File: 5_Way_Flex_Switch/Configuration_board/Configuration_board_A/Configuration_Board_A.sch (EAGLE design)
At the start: 1 part

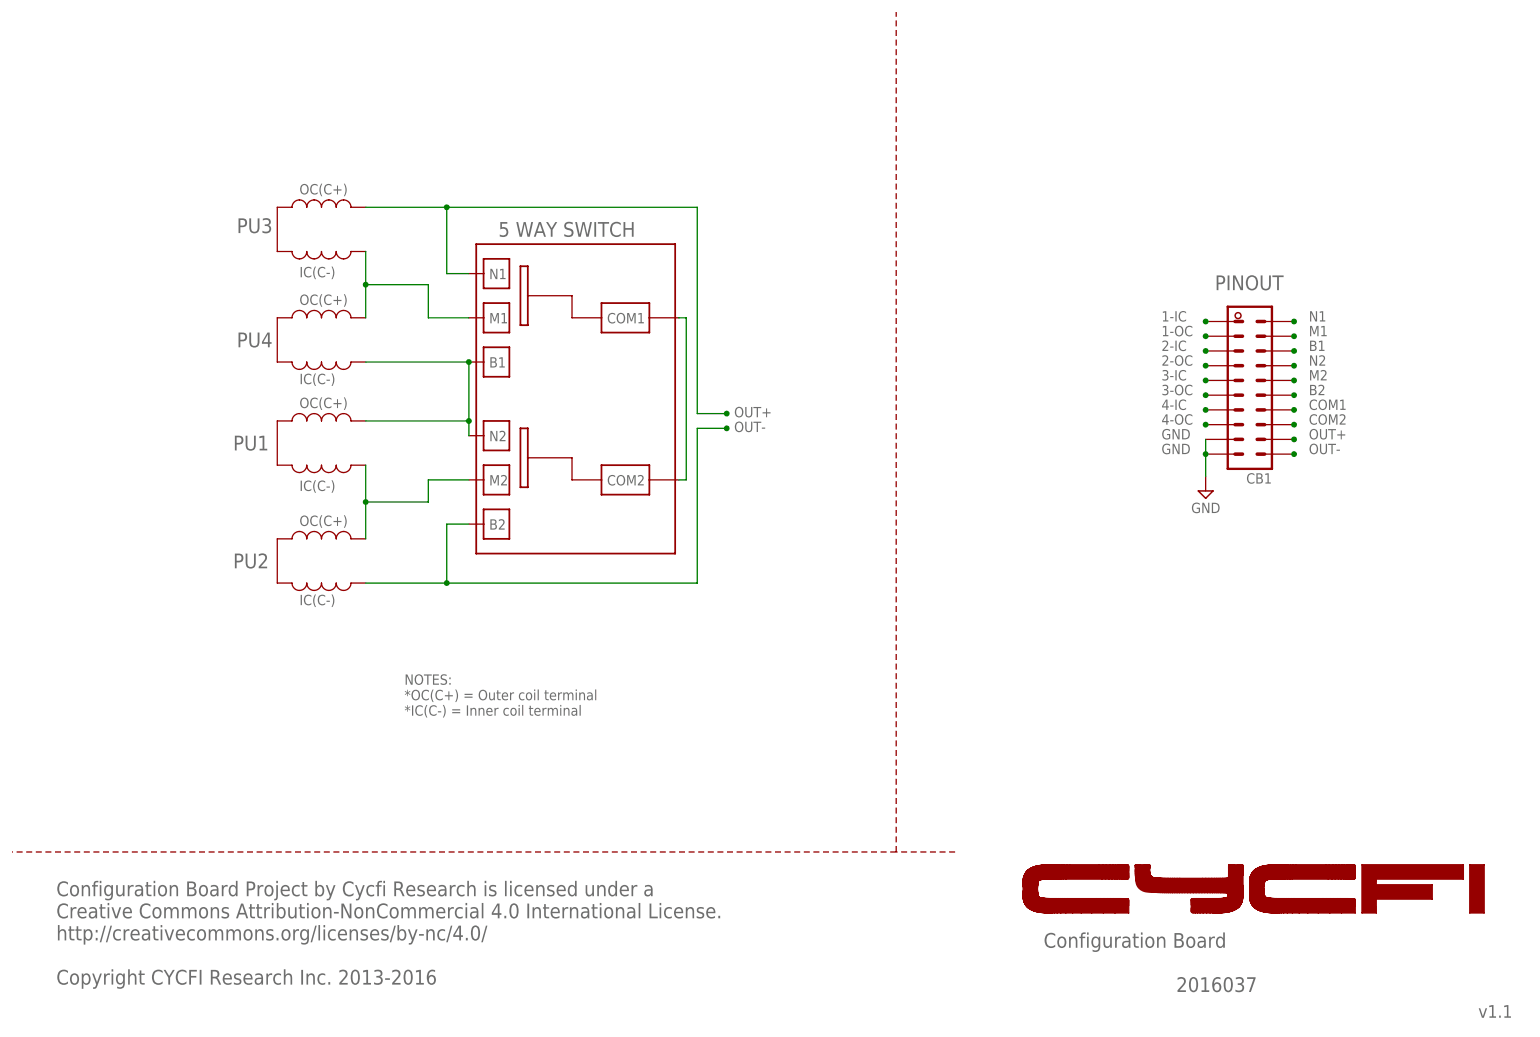
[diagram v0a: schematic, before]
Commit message: *organize 5-waay switch and its configuration board(a and b) *update license date *remove red frame schem pdf files, change with black frame *update document number
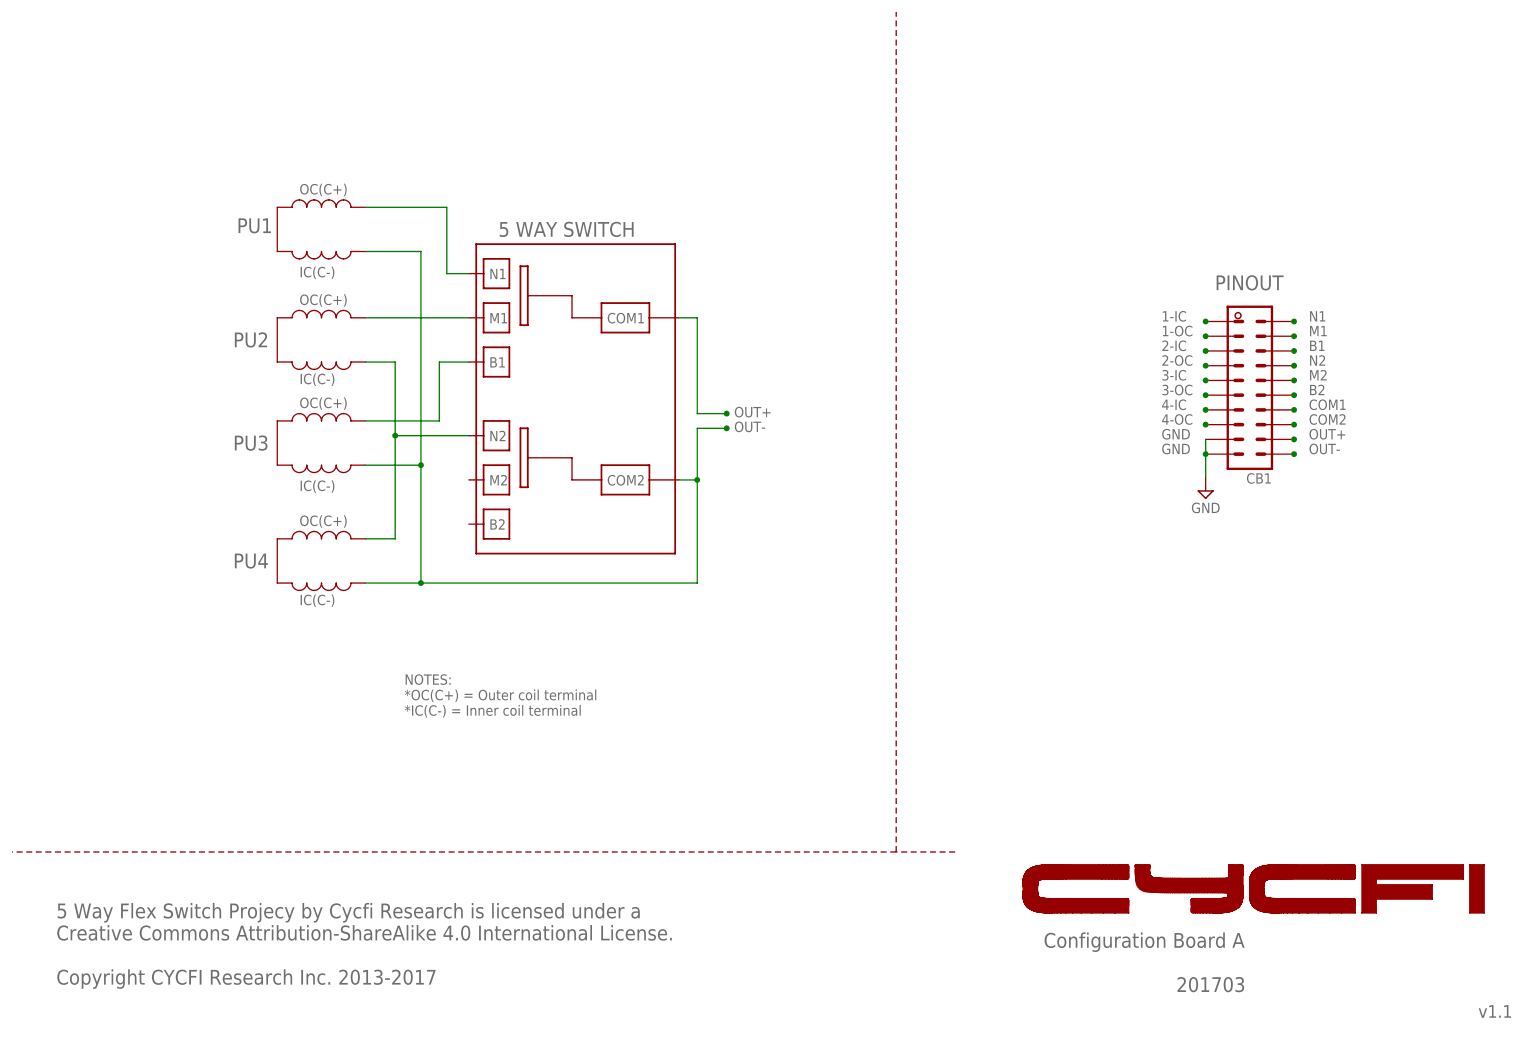
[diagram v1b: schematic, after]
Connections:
- removed net 1: CB1.3-OC, CB1.N1, CB1.OUT+
- removed net 2: CB1.3-IC, CB1.4-OC, CB1.M1
- removed net 3: CB1.1-OC, CB1.4-IC, CB1.B1, CB1.N2
- removed net 4: CB1.COM1, CB1.COM2
- removed net 5: CB1.1-IC, CB1.2-OC, CB1.M2
- removed net GND: CB1.GND, CB1.GND1
- new net B1: CB1.3-OC, CB1.B1
- new net B2: CB1.B2
- new net M1: CB1.2-OC, CB1.M1
- new net M2: CB1.M2
- new net N1: CB1.1-OC, CB1.N1
- new net N2: CB1.2-IC, CB1.4-OC, CB1.N2
- new net O+: CB1.COM1, CB1.OUT+
- new net O-: CB1.1-IC, CB1.3-IC, CB1.4-IC, CB1.COM2, CB1.OUT-
- net 6: now also CB1.GND, CB1.GND1; no longer CB1.2-IC, CB1.B2, CB1.OUT-
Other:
- note added: "201703"
- note added: "5 Way Flex Switch Projecy by Cycfi Research is licensed under a Creative Commons Attribution-ShareAlike 4.0 International License. Copyright CYCFI Research Inc. 2013-2017"
- note added: "Configuration Board A"
- note removed: "2016037"
- note removed: "Configuration Board"
- note removed: "Configuration Board Project by Cycfi Research is licensed under a Creative Commons Attribution-NonCommercial 4.0 International License. http://creativecommons.org/licenses/by-nc/4.0/ Copyright CYCFI Research Inc. 2013-2016"

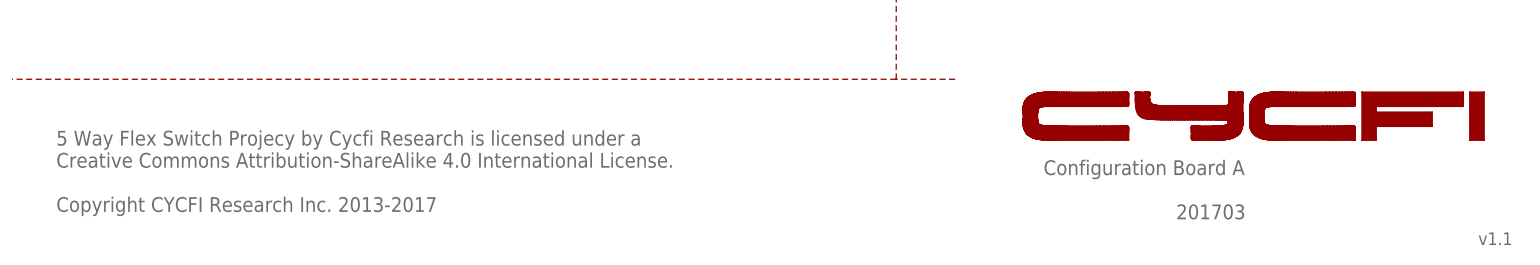
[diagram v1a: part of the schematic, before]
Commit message: Updated broken .sch files
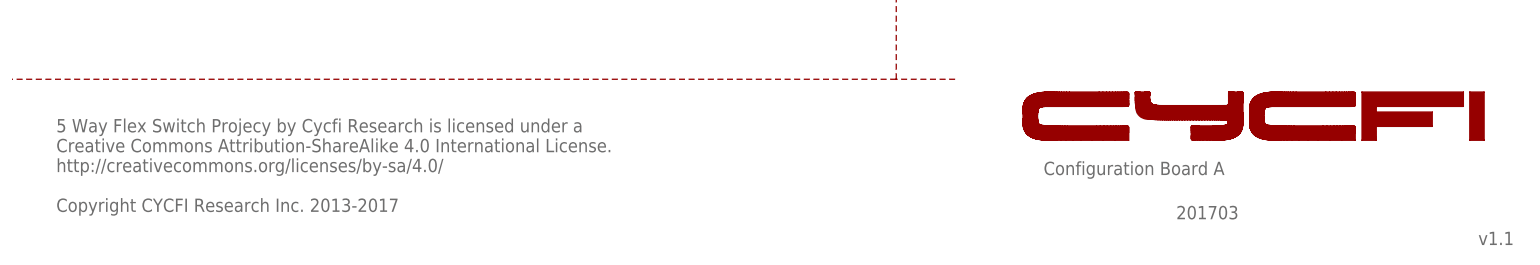
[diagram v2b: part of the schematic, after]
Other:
- note added: "5 Way Flex Switch Projecy by Cycfi Research is licensed under a Creative Commons Attribution-ShareAlike 4.0 International License. http://creativecommons.org/licenses/by-sa/4.0/ Copyright CYCFI Research Inc. 2013-2017"
- note removed: "5 Way Flex Switch Projecy by Cycfi Research is licensed under a Creative Commons Attribution-ShareAlike 4.0 International License. Copyright CYCFI Research Inc. 2013-2017"
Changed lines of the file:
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@@
 <text x="38.1" y="104.775" size="2.54" layer="95">PU3</text>
 <text x="38.1" y="84.455" size="2.54" layer="95">PU4</text>
-<text x="177.8" y="19.05" size="2.54" layer="95">Configuration Board A</text>
-<text x="252.73" y="6.985" size="2.1844" layer="95">v1.1</text>
-<text x="7.62" y="12.7" size="2.54" layer="95">5 Way Flex Switch Projecy by Cycfi Research is licensed under a
+<text x="177.8" y="19.05" size="2.286" layer="95">Configuration Board A</text>
+<text x="252.73" y="6.985" size="2.286" layer="95">v1.1</text>
+<text x="7.62" y="12.7" size="2.286" layer="95">5 Way Flex Switch Projecy by Cycfi Research is licensed under a
 Creative Commons Attribution-ShareAlike 4.0 International License.
+http://creativecommons.org/licenses/by-sa/4.0/
 Copyright CYCFI Research Inc. 2013-2017</text>
-<text x="200.66" y="11.43" size="2.54" layer="95">201703</text>
+<text x="200.66" y="11.43" size="2.286" layer="95">201703</text>
 <wire x1="192.47528125" y1="25.047221875" x2="190.115640625" y2="25.047221875" width="0" layer="94"/>
 <wire x1="190.115640625" y1="25.047221875" x2="188.10833125" y2="25.047225" width="0" layer="94"/>
@@
 <instance part="FRAME1" gate="G$1" x="0" y="0"/>
 <instance part="FRAME1" gate="G$2" x="162.56" y="0" smashed="yes">
-<attribute name="LAST_DATE_TIME" x="175.26" y="1.27" size="2.54" layer="94" font="vector"/>
-<attribute name="SHEET" x="248.92" y="1.27" size="2.54" layer="94" font="vector"/>
+<attribute name="LAST_DATE_TIME" x="175.26" y="1.27" size="2.286" layer="94" font="vector"/>
+<attribute name="SHEET" x="248.92" y="1.27" size="2.286" layer="94" font="vector"/>
 </instance>
 <instance part="SUPPLY3" gate="GND" x="205.74" y="97.79" smashed="yes" rot="MR0">
